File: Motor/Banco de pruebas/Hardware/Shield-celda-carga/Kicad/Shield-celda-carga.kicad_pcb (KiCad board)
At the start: 2 copper layers, 54.6 x 49.5 mm, 16 parts, among them J1 Conexion bateria, J2 Screw_Terminal_01x03, J3 Conn_01x04, J4 Alimentacion Arduino, K1 Rele 12V-360mW, Q1 BC337

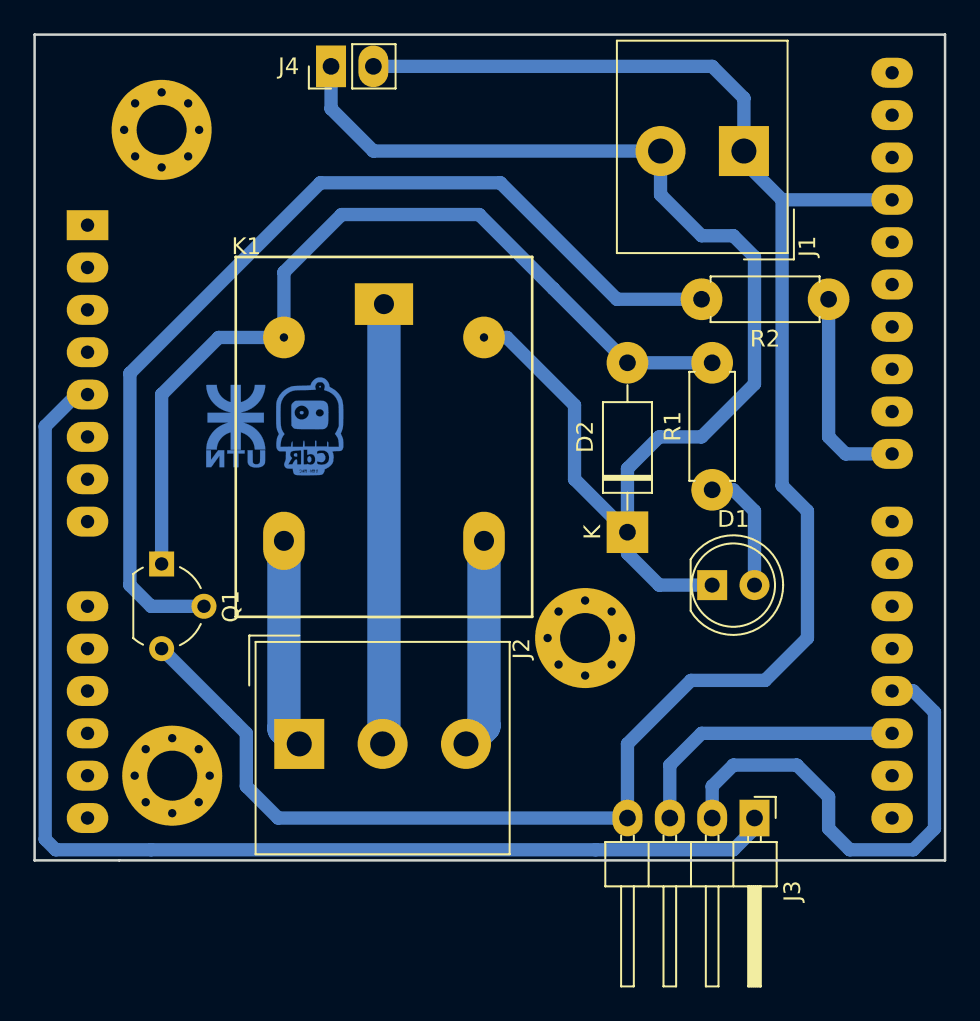
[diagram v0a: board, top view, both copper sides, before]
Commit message: Se agrego un circuito RC en la base del transistor del rele por problemas de ruiido al resetear y se creo la Rev2
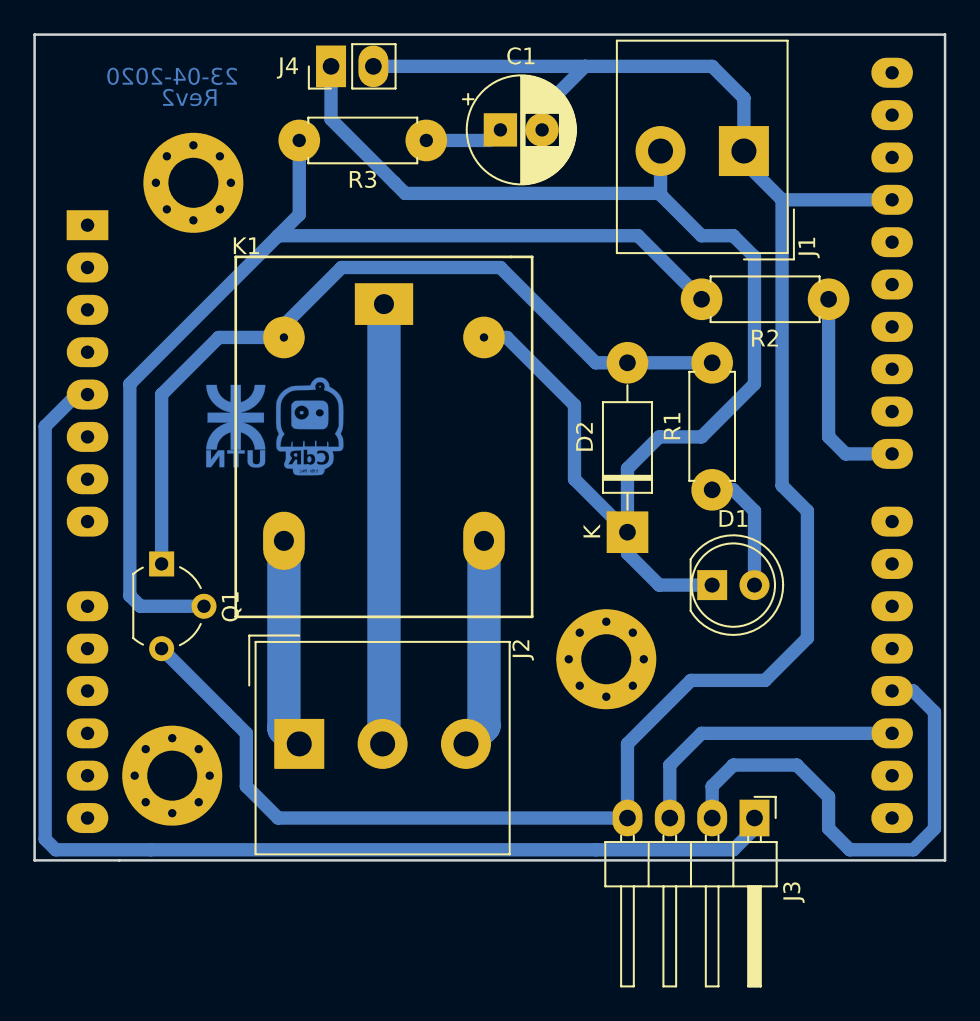
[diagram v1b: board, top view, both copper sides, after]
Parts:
- added C1: 100uf, Capacitor_THT:CP_Radial_D6.3mm_P2.50mm, F.Cu at (57.1, 48.3)
- added R3: 10k, Resistor_THT:R_Axial_DIN0207_L6.3mm_D2.5mm_P7.62mm_Horizontal, F.Cu at (52.7, 48.9)
- R2: value 560 -> 10k
- moved ? 3.70 mm to (38.7, 51.4)
- moved ? 1.80 mm to (63.5, 80.0)
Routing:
- net GND: track 115.5 -> 120.3 mm
- net Net-(C1-Pad1): track 0.00 -> 4.71 mm
- net Net-(D2-Pad2): track 53.6 -> 49.1 mm
- net Net-(Q1-Pad2): track 59.6 -> 63.2 mm
- net +12V: track 77.5 -> 79.0 mm
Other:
- board text added: "23-04-2020"
- board text added: "Rev2"
